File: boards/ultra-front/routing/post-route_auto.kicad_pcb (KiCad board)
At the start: 2 copper layers, 110 x 40 mm, 40 parts, among them J1 FPC-05F-20PH20, J2 FPC-05FB-12PH20, Q1 AO3400A, SW1 TS-1187A-B-A-B, SW2 TS-1187A-B-A-B, SW3 TS-1187A-B-A-B, SW4 EC11E1834403, U1 TCA9535PWR, U2 IRM-H638T/TR2

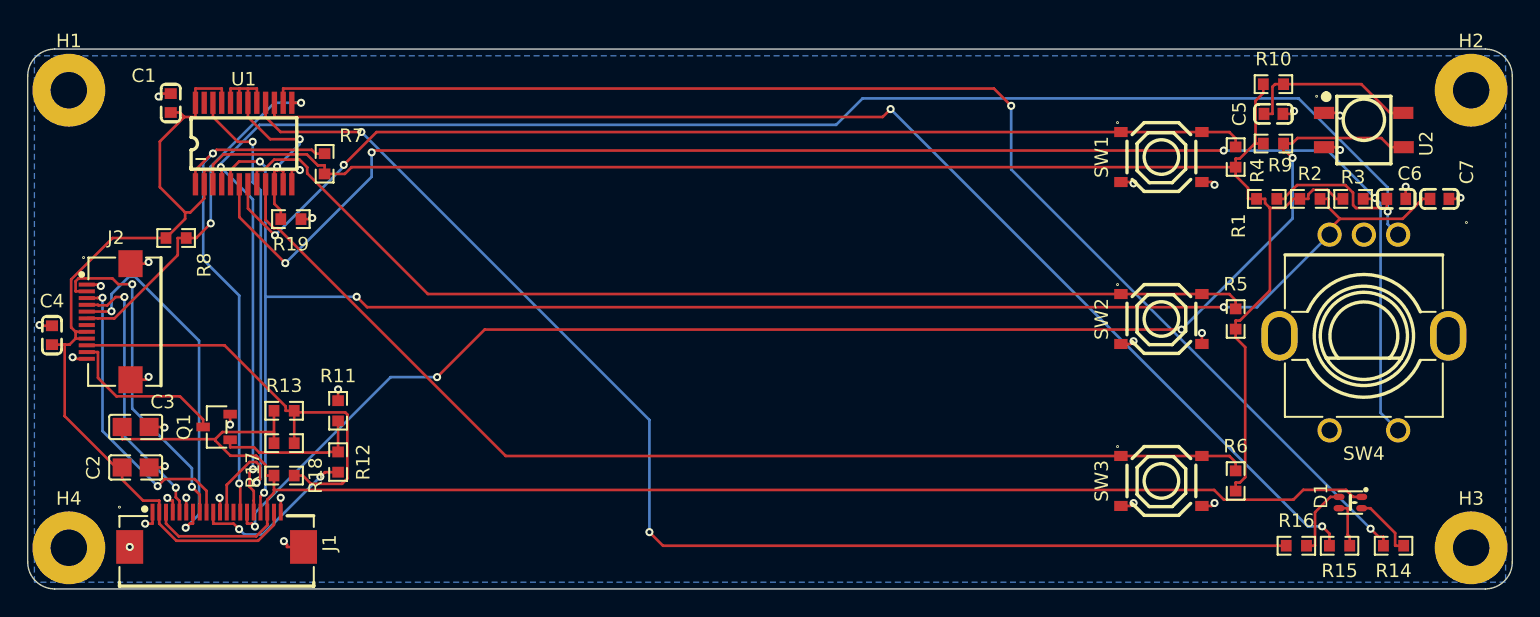
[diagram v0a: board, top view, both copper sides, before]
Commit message: ultra-front: fix LCD tail seating and keepouts from board review, re-route (GND as a net, edge keepout), docs and learnings
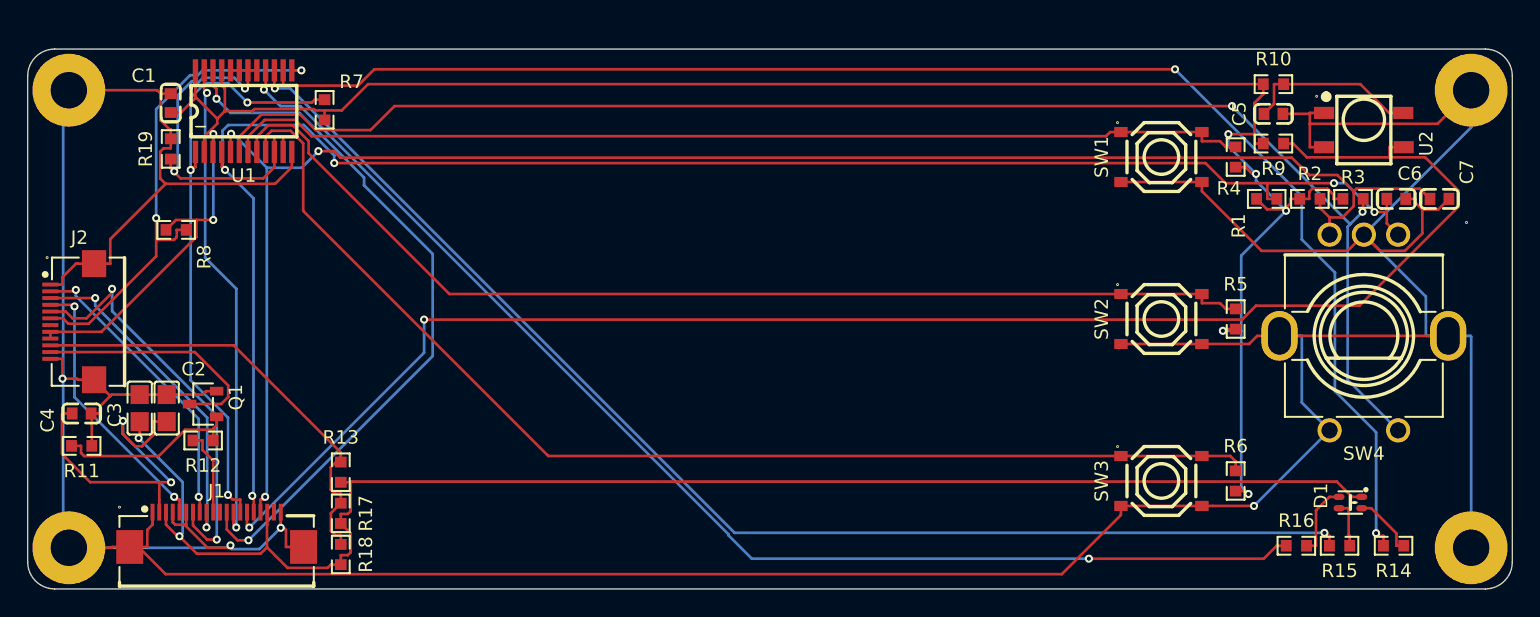
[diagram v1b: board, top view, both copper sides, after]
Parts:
- moved R11 19.2 mm to (-5.95, 56.2), turned to 0 degrees
- moved R19 10.3 mm to (0.66, 34.2), turned to 90 degrees
- moved R12 10.1 mm to (3.06, 55.8), turned to 0 degrees
- moved R18 7.20 mm to (13.3, 64.2), turned to 90 degrees
- moved R17 6.68 mm to (13.3, 61.2), turned to 90 degrees
- moved C4 6.20 mm to (-5.95, 53.8), turned to 0 degrees
- moved R13 6.19 mm to (13.3, 58.1), turned to 90 degrees
- moved C2 4.96 mm to (0.35, 53.4), turned to 90 degrees
- moved R7 4.00 mm to (12.1, 31.3)
- moved J2 2.70 mm to (-6.64, 47.0)
- moved U1 2.40 mm to (6.05, 31.4)
- moved Q1 1.97 mm to (3.06, 53.1)
- moved C3 1.43 mm to (-1.65, 53.4), turned to 90 degrees
- moved R8 0.60 mm to (1.05, 40.2)
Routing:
- net GND: track 32.3 -> 351.5 mm, vias 30 -> 4
- net /I2C_SDA: track 0.00 -> 36.2 mm, vias 0 -> 2
- net /I2C_SCL: track 37.0 -> 53.4 mm
- net /IR_OUT: track 103.8 -> 119.5 mm, vias 4 -> 2
- net /LCD_RST: track 26.4 -> 36.5 mm
- net /LED_R: track 99.7 -> 109.6 mm
- net +3V3: track 187.9 -> 197.3 mm, vias 0 -> 9
- net /ENC_A: track 134.2 -> 125.1 mm, vias 3 -> 5
- net /EXP_UNUSED: track 20.2 -> 28.5 mm
- net /LCD_BL_PWM: track 12.3 -> 6.34 mm, vias 2 -> 0
- net /FRONT_INT_N: track 39.4 -> 45.2 mm, vias 2 -> 3
- net /BL_K: track 12.4 -> 18.1 mm
- net /ENC_SW: track 112.8 -> 108.1 mm, vias 4 -> 2
- net /BTN3: track 82.6 -> 87.0 mm
- net /BTN1: track 79.9 -> 76.3 mm, vias 2 -> 0
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- removed copper zone on B.Cu, net GND
